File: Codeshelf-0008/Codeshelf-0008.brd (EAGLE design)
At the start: 140.5 x 104 mm, 43 parts, among them IC1 74AHC1G04DCK, IC2 74AHC1G04DCK, IC4 74AHC1G08DCK, IC5 74AHC1G08DCK, IC6 74AHC1G08DCK, J1 M05X2PTH, J2 POWER_JACKPTH, J3 M08X2, J4 M08X2, Q1 MOSFET-NCHANNELBSS138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

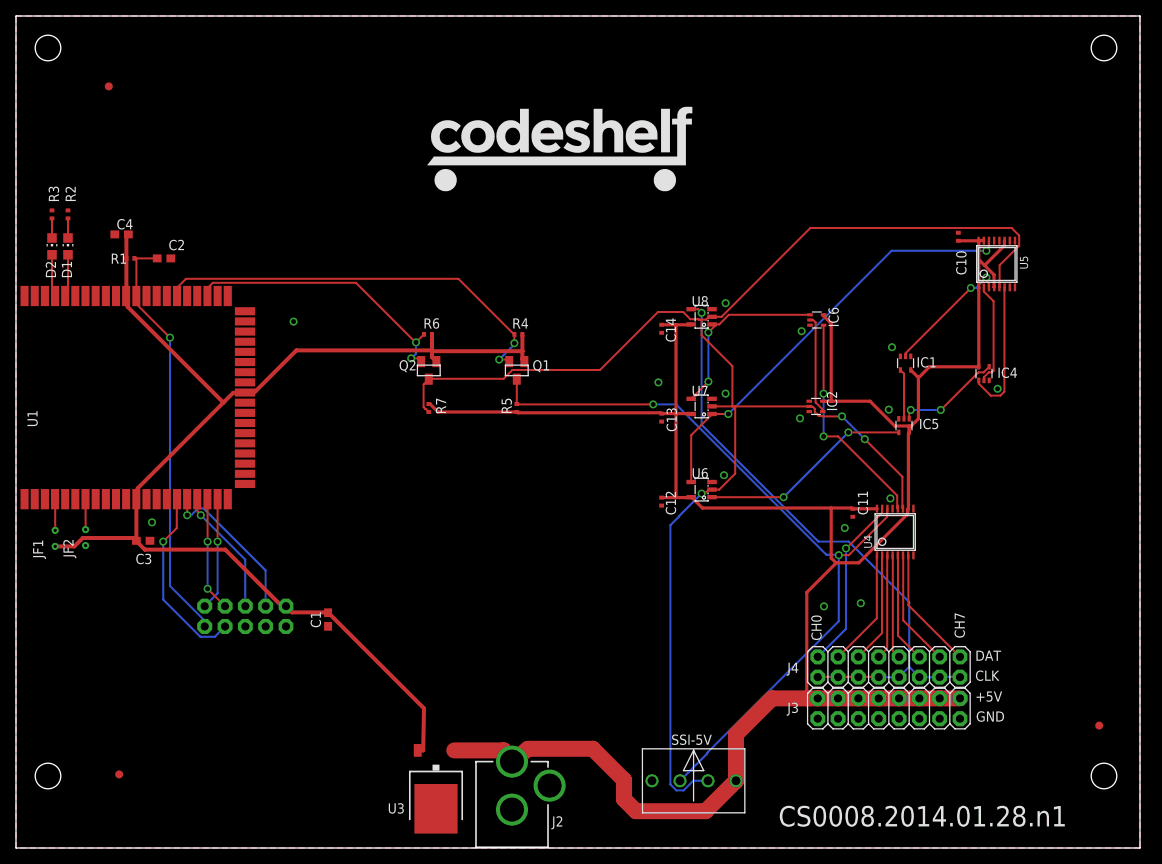
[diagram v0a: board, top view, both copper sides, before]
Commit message: Aisle Controller release
Deleted old files (post-earlier commit), renamed to lose version
numbering. This is tag / version CS0008.v3.
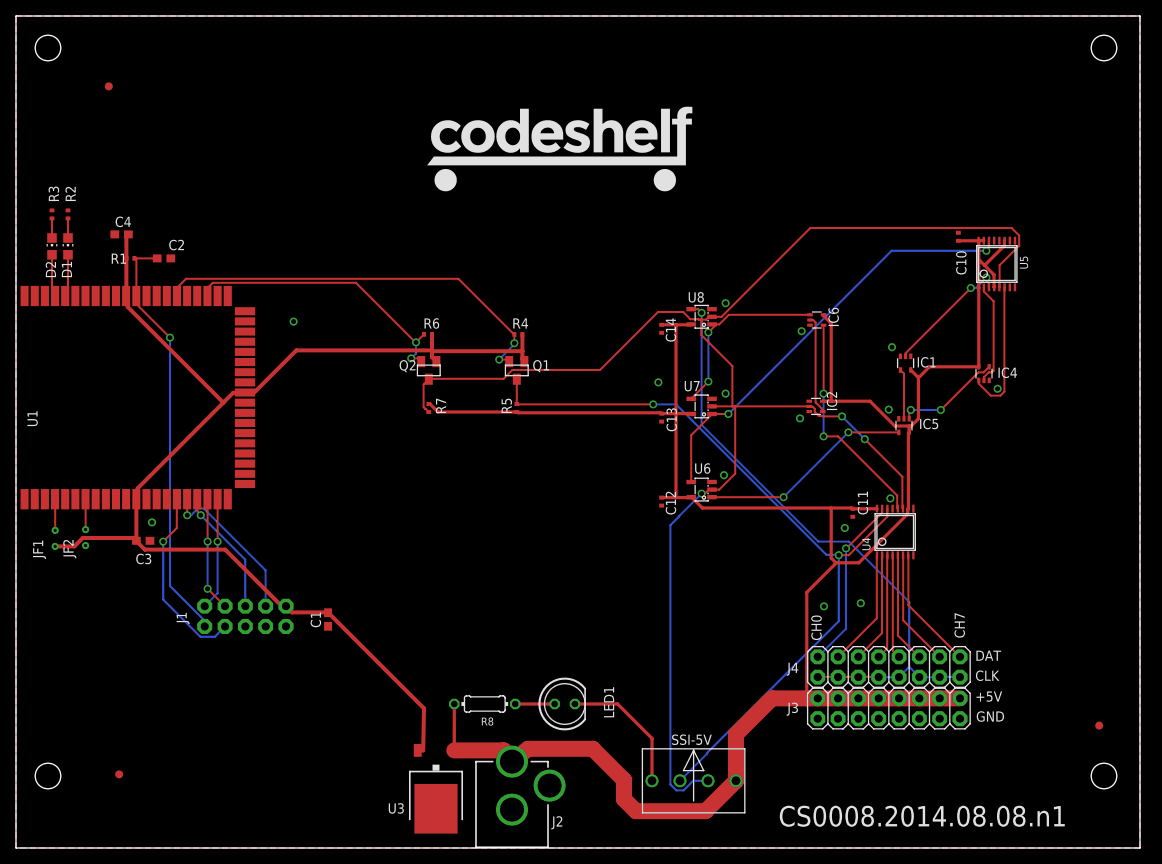
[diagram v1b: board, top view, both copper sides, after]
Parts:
- added LED1: BLUE, led:LED5MM
- added R8: 1K, rcl:0204/7
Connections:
- new net N$5: LED1.A, R8.1
- net +5V: now also R8.2
- net GND: now also LED1.K
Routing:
- net GND: track 0.00 -> 16.7 mm
- net +5V: track 279.3 -> 285.1 mm
- net N$5: track 0.00 -> 4.92 mm
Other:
- board text added: "CS0008.2014.08.08.n1"
- board text removed: "CS0008.2014.01.28.n1"
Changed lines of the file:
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@@
 <text x="100.7" y="25.9" size="1.27" layer="21" rot="R90">CH0</text>
 <text x="118.6" y="26.2" size="1.27" layer="21" rot="R90">CH7</text>
-<text x="95.3" y="2.7" size="2.54" layer="21">CS0008.2014.01.28.n1</text>
+<text x="95.3" y="2.7" size="2.54" layer="21">CS0008.2014.08.08.n1</text>
 <hole x="4" y="100" drill="3.2"/>
 <hole x="136" y="100" drill="3.2"/>
@@
 </element>
 <element name="J1" library="SparkFun" package="AVR_ICSP" value="M05X2PTH" x="28.67" y="28.96" smashed="yes" rot="MR270">
-<attribute name="NAME" x="21.572" y="28.454" size="1.27" layer="26" rot="MR0"/>
+<attribute name="NAME" x="21.346" y="28.072" size="1.27" layer="25" rot="R90"/>
 <attribute name="NOTES" value="DNP - flashing header" x="28.67" y="28.96" size="1.778" layer="28" rot="MR270" display="off"/>
 </element>
@@
 <attribute name="NAME" x="5" y="71.2" size="1.27" layer="25" rot="R90"/>
 <attribute name="MFGN" value="OSRAM" x="4.5" y="75.2" size="1.778" layer="27" display="off"/>
-<attribute name="MFGP" value="Q65110P5179" x="4.5" y="75.2" size="1.778" layer="27" display="off"/>
+<attribute name="MFGP" value="LG R971-KN-1" x="4.5" y="75.2" size="1.778" layer="27" display="off"/>
 <attribute name="NOTES" value="DNP" x="4.5" y="75.2" size="1.778" layer="27" display="off"/>
 </element>
@@
 </element>
 <element name="C4" library="GW-devices" package="C0603" value="100pF" x="13.2" y="76.7" smashed="yes">
-<attribute name="NAME" x="12.565" y="77.335" size="1.27" layer="25"/>
+<attribute name="NAME" x="12.365" y="77.635" size="1.27" layer="25"/>
 <attribute name="MFGN" value="Murata" x="13.2" y="76.7" size="1.778" layer="27" display="off"/>
 <attribute name="MFGP" value="C0603C101K5RACTU" x="13.2" y="76.7" size="1.778" layer="27" display="off"/>
@@
 <element name="J2" library="GW-devices" package="POWER_JACK_PTH" value="POWER_JACKPTH" x="62" y="-2.9" smashed="yes">
 <attribute name="NAME" x="66.99" y="2.68" size="1.27" layer="25"/>
-<attribute name="MFG" value="Kobiconn" x="62" y="-2.9" size="1.778" layer="27" display="off"/>
 <attribute name="MFGP" value="163-7620-E" x="62" y="-2.9" size="1.778" layer="27" display="off"/>
+<attribute name="MFGN" value="Kobiconn" x="62" y="-2.9" size="1.778" layer="27" display="off"/>
 </element>
 <element name="SSI-5V" library="GW-devices" package="MOLEX-39357-0004" value="HEADER-4X39357" x="84.7" y="8.4" smashed="yes">
@@
 </element>
 <element name="U4" library="GW-devices" package="TSSOP16" value="SN74HC595PW" x="109.9" y="39.5" smashed="yes">
-<attribute name="NAME" x="107.0044" y="37.4172" size="1.016" layer="25" ratio="10" rot="R90"/>
+<attribute name="NAME" x="106.8044" y="37.1172" size="1.016" layer="25" ratio="10" rot="R90"/>
 <attribute name="MFGN" value="TI" x="109.9" y="39.5" size="1.778" layer="27" display="off"/>
 <attribute name="MFGP" value="SN74HC595PWR" x="109.9" y="39.5" size="1.778" layer="27" display="off"/>
@@
 </element>
 <element name="U6" library="GW-devices" package="SOT23-5" value="D-FLIP-FLOP-74LV1G79DBVR" x="85.7" y="44.8" smashed="yes" rot="R90">
-<attribute name="NAME" x="84.45" y="46.2" size="1.27" layer="25"/>
+<attribute name="NAME" x="84.75" y="46.8" size="1.27" layer="25"/>
 <attribute name="MFGN" value="TI" x="85.7" y="44.8" size="1.778" layer="27" rot="R90" display="off"/>
 <attribute name="MFGP" value="SN74LVC1G79DBVR" x="85.7" y="44.8" size="1.778" layer="27" rot="R90" display="off"/>
@@
 </element>
 <element name="U7" library="GW-devices" package="SOT23-5" value="D-FLIP-FLOP-74LV1G79DBVR" x="85.7" y="55.2" smashed="yes" rot="R90">
-<attribute name="NAME" x="84.45" y="56.5" size="1.27" layer="25"/>
+<attribute name="NAME" x="83.45" y="57.1" size="1.27" layer="25"/>
 <attribute name="MFGN" value="TI" x="85.7" y="55.2" size="1.778" layer="27" rot="R90" display="off"/>
 <attribute name="MFGP" value="SN74LVC1G79DBVR" x="85.7" y="55.2" size="1.778" layer="27" rot="R90" display="off"/>
@@
 </element>
 <element name="U8" library="GW-devices" package="SOT23-5" value="D-FLIP-FLOP-74LV1G79DBVR" x="85.7" y="66.4" smashed="yes" rot="R90">
-<attribute name="NAME" x="84.45" y="67.7" size="1.27" layer="25"/>
+<attribute name="NAME" x="83.95" y="68.2" size="1.27" layer="25"/>
 <attribute name="MFGN" value="TI" x="85.7" y="66.4" size="1.778" layer="27" rot="R90" display="off"/>
 <attribute name="MFGP" value="SN74LVC1G79DBVR" x="85.7" y="66.4" size="1.778" layer="27" rot="R90" display="off"/>
@@
 <element name="U$3" library="adafruit" package="FIDUCIAL_1MM" value="FIDUCIAL" x="11.6" y="95.2"/>
 <element name="U$4" library="adafruit" package="FIDUCIAL_1MM" value="FIDUCIAL" x="135.4" y="15.3"/>
+<element name="LED1" library="led" package="LED5MM" value="BLUE" x="68.6" y="18" smashed="yes">
+<attribute name="MFGN" value="Cree Inc" x="68.6" y="18" size="1.778" layer="27" display="off"/>
+<attribute name="MFGP" value="C503B-BCN-CV0Z0461" x="68.6" y="18" size="1.778" layer="27" display="off"/>
+<attribute name="NAME" x="74.7666" y="16.175" size="1.27" layer="25" ratio="10" rot="R90"/>
+</element>
+<element name="R8" library="rcl" package="0204/7" value="1K" x="58.6" y="18" smashed="yes" rot="R180">
+<attribute name="MFGN" value="Stackpole Electronics Inc" x="58.6" y="18" size="1.778" layer="27" rot="R180" display="off"/>
+<attribute name="MFGP" value="CF18JT1K00" x="58.6" y="18" size="1.778" layer="27" rot="R180" display="off"/>
+<attribute name="NAME" x="59.74" y="16.3046" size="0.9906" layer="25" ratio="10" rot="R180"/>
+<attribute name="VALUE" x="60.2256" y="18.4826" size="0.9906" layer="27" ratio="10" rot="R180"/>
+</element>
 </elements>
 <signals>
@@
 <via x="105.6" y="30.6" extent="1-16" drill="0.6096"/>
 <via x="101" y="30.2" extent="1-16" drill="0.6096"/>
+<contactref element="LED1" pad="K"/>
+<wire x1="69.87" y1="18" x2="75.2" y2="18" width="0.4064" layer="1"/>
+<wire x1="75.2" y1="18" x2="79.5" y2="13.7" width="0.4064" layer="1"/>
+<wire x1="79.5" y1="13.7" x2="79.5" y2="8.4" width="0.4064" layer="1"/>
 </signal>
 <signal name="+3V3" class="1">
@@
 <wire x1="90" y1="14.2" x2="94.5" y2="18.7" width="2" layer="1"/>
 <wire x1="94.5" y1="18.7" x2="98.85" y2="18.7" width="2" layer="1"/>
+<contactref element="R8" pad="2"/>
+<wire x1="54.79" y1="18" x2="54.78" y2="12.2" width="0.4064" layer="1"/>
 </signal>
 <signal name="SSI-TX-3V3">
@@
 <wire x1="102.8" y1="23.9" x2="102.76" y2="23.9" width="0.254" layer="1"/>
 </signal>
+<signal name="N$5">
+<contactref element="LED1" pad="A"/>
+<contactref element="R8" pad="1"/>
+<wire x1="62.41" y1="18" x2="67.33" y2="18" width="0.4064" layer="1"/>
+</signal>
 </signals>
